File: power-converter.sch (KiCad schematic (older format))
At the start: 16 parts

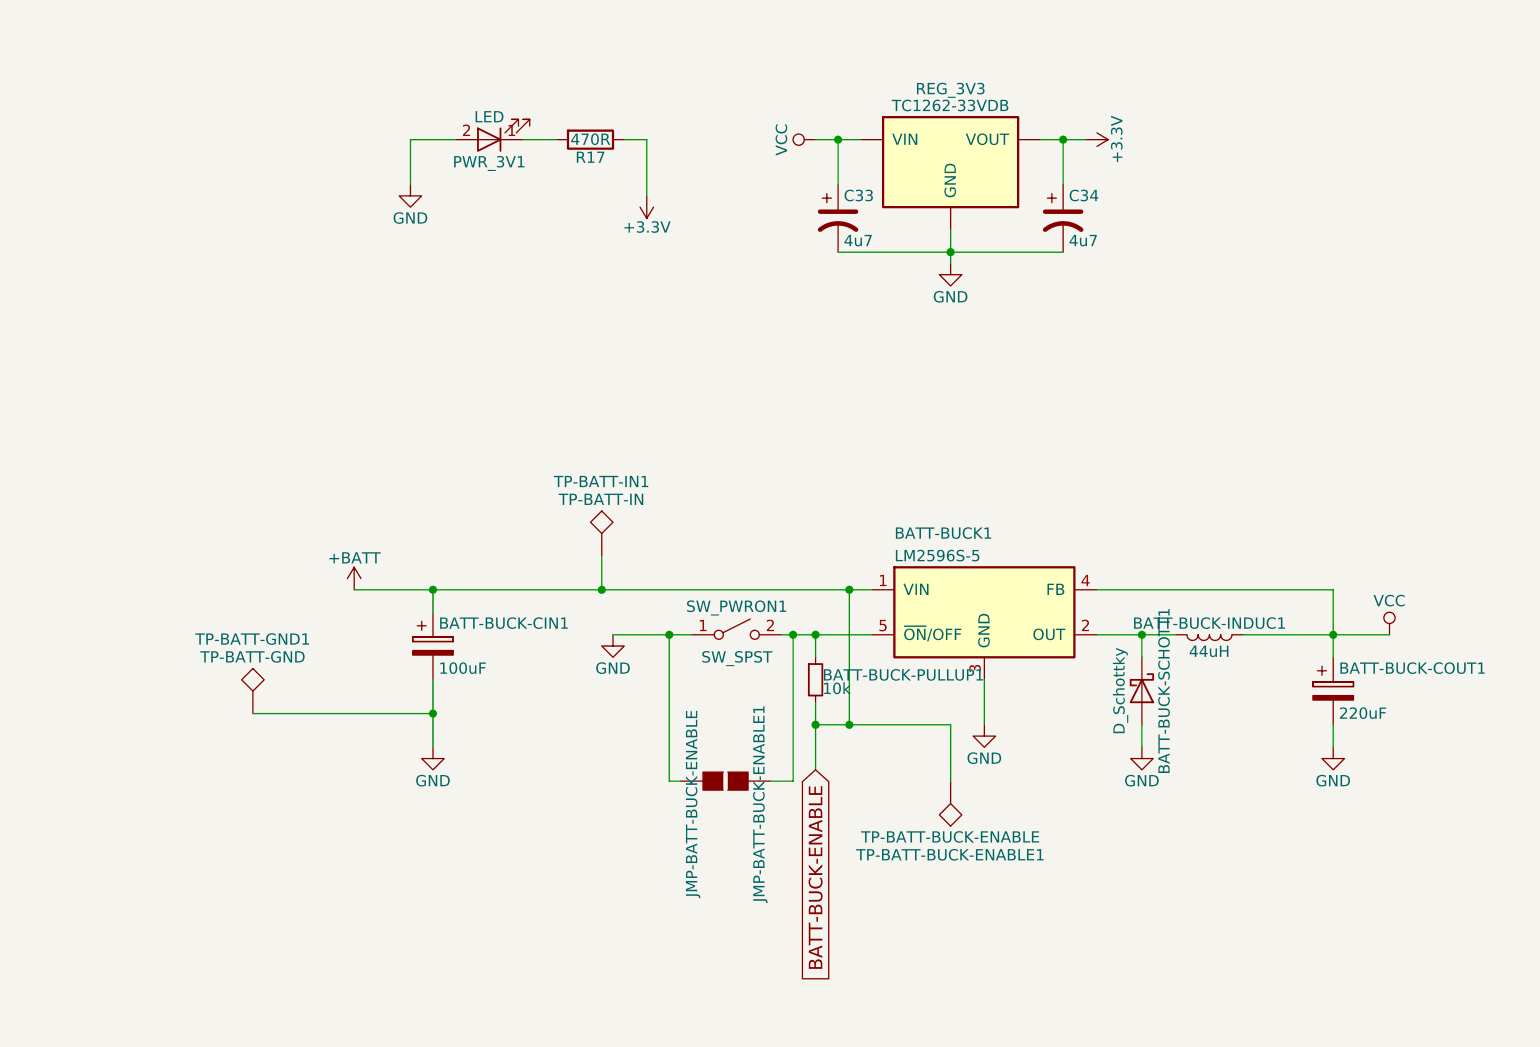
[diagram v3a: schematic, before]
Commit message: splitting led power out from 5v so that we can insert the mosfet
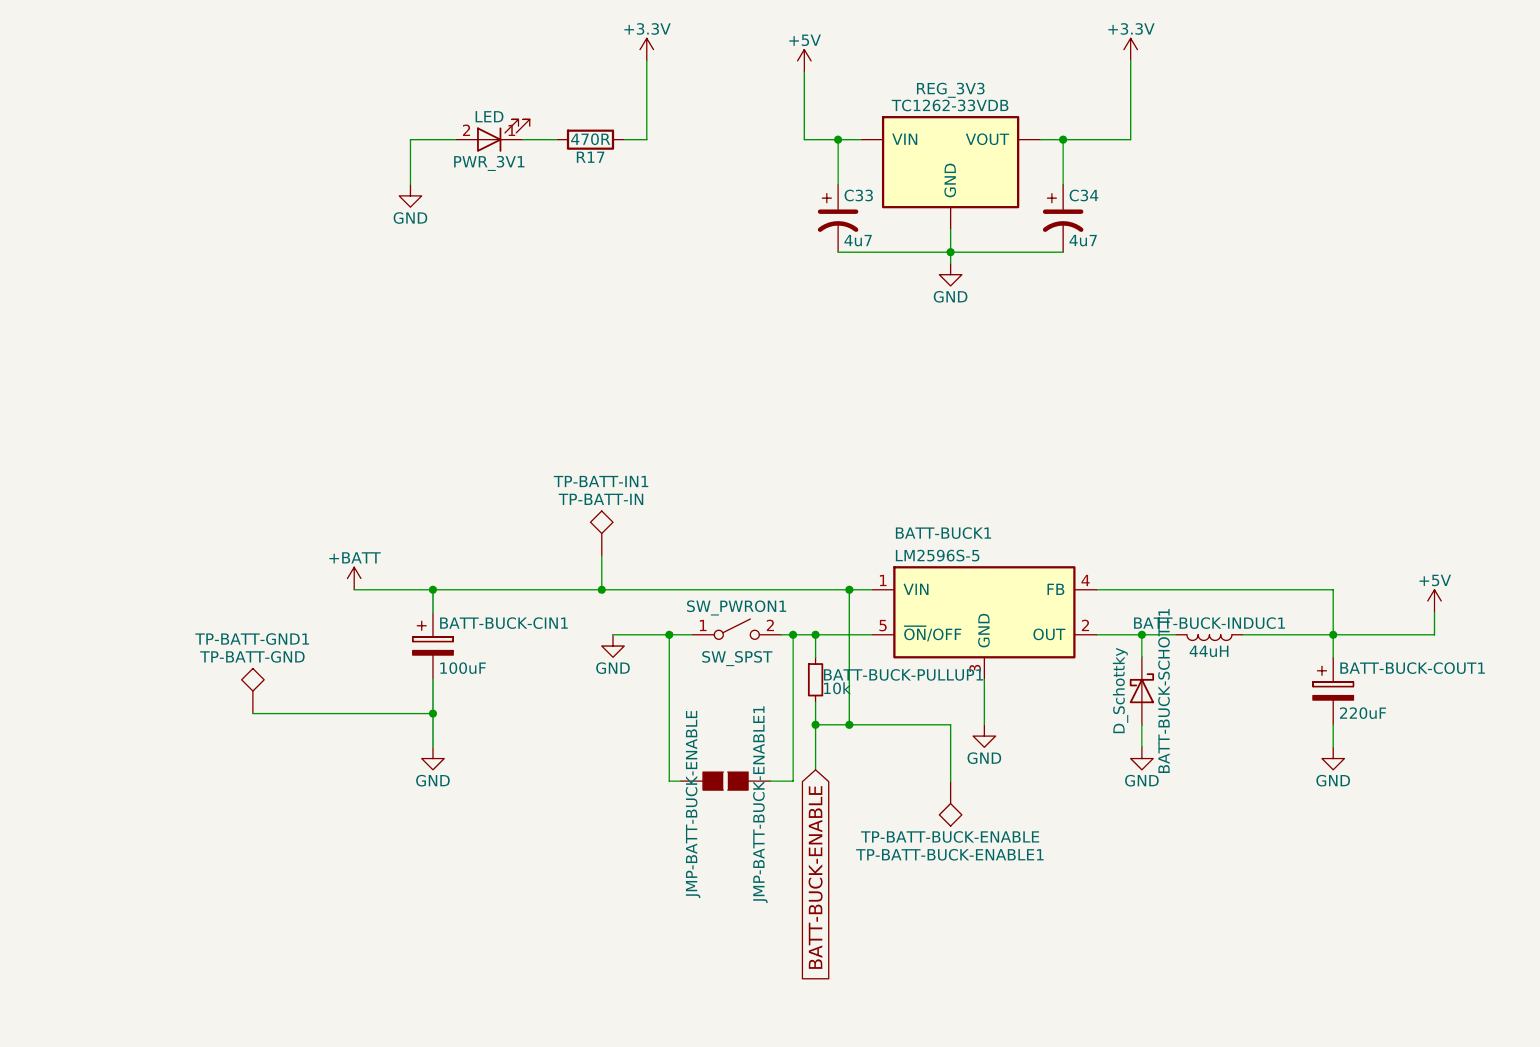
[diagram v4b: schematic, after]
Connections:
- net VCC renamed +5V
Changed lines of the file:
@@
 	5750 3900 6150 3900
 $Comp
-L GND #PWR025
+L GND #PWR27
 U 1 1 5B2D2C35
 P 5000 3900
-F 0 "#PWR025" H 5000 3650 50  0001 C CNN
+F 0 "#PWR27" H 5000 3650 50  0001 C CNN
 F 1 "GND" H 5000 3750 50  0000 C CNN
 F 2 "" H 5000 3900 50  0001 C CNN
@@
 Wire Wire Line
 	7150 3900 7500 3900
-$Comp
-L VCC #PWR026
-U 1 1 5B2D2C44
-P 8450 3900
-F 0 "#PWR026" H 8450 3750 50  0001 C CNN
-F 1 "VCC" H 8450 4050 50  0000 C CNN
-F 2 "" H 8450 3900 50  0001 C CNN
-F 3 "" H 8450 3900 50  0001 C CNN
-	1    8450 3900
-	1    0    0    -1
-$EndComp
-Wire Wire Line
-	7800 3900 8450 3900
+Wire Wire Line
+	7800 3900 8650 3900
 Wire Wire Line
 	7150 3700 8200 3700
@@
 Connection ~ 8200 3900
 $Comp
-L GND #PWR027
+L GND #PWR33
 U 1 1 5B2D2C55
 P 7350 4400
-F 0 "#PWR027" H 7350 4150 50  0001 C CNN
+F 0 "#PWR33" H 7350 4150 50  0001 C CNN
 F 1 "GND" H 7350 4250 50  0000 C CNN
 F 2 "" H 7350 4400 50  0001 C CNN
@@
 $EndComp
 $Comp
-L GND #PWR028
+L GND #PWR34
 U 1 1 5B2D2C63
 P 8200 4400
-F 0 "#PWR028" H 8200 4150 50  0001 C CNN
+F 0 "#PWR34" H 8200 4150 50  0001 C CNN
 F 1 "GND" H 8200 4250 50  0000 C CNN
 F 2 "" H 8200 4400 50  0001 C CNN
@@
 	8200 4300 8200 4400
 $Comp
-L GND #PWR029
+L GND #PWR31
 U 1 1 5B2D2C6A
 P 6650 4300
-F 0 "#PWR029" H 6650 4050 50  0001 C CNN
+F 0 "#PWR31" H 6650 4050 50  0001 C CNN
 F 1 "GND" H 6650 4150 50  0000 C CNN
 F 2 "" H 6650 4300 50  0001 C CNN
@@
 	3850 3700 6150 3700
 $Comp
-L GND #PWR030
+L GND #PWR26
 U 1 1 5B2D2C79
 P 4200 4400
-F 0 "#PWR030" H 4200 4150 50  0001 C CNN
+F 0 "#PWR26" H 4200 4150 50  0001 C CNN
 F 1 "GND" H 4200 4250 50  0000 C CNN
 F 2 "" H 4200 4400 50  0001 C CNN
@@
 Connection ~ 6050 4300
 $Comp
-L +BATT #PWR031
+L +BATT #PWR24
 U 1 1 5B2D2CA5
 P 3850 3700
-F 0 "#PWR031" H 3850 3550 50  0001 C CNN
+F 0 "#PWR24" H 3850 3550 50  0001 C CNN
 F 1 "+BATT" H 3850 3840 50  0000 C CNN
 F 2 "" H 3850 3700 50  0001 C CNN
@@
 Connection ~ 4200 4250
 $Comp
-L +3.3V #PWR032
+L +3.3V #PWR28
 U 1 1 5B2DAE29
-P 5150 1950
-F 0 "#PWR032" H 5150 1800 50  0001 C CNN
-F 1 "+3.3V" H 5150 2090 50  0000 C CNN
-F 2 "" H 5150 1950 50  0001 C CNN
-F 3 "" H 5150 1950 50  0001 C CNN
-	1    5150 1950
-	-1   0    0    1
+P 5150 1350
+F 0 "#PWR28" H 5150 1200 50  0001 C CNN
+F 1 "+3.3V" H 5150 1490 50  0000 C CNN
+F 2 "" H 5150 1350 50  0001 C CNN
+F 3 "" H 5150 1350 50  0001 C CNN
+	1    5150 1350
+	1    0    0    -1
 $EndComp
 $Comp
@@
 $EndComp
 $Comp
-L +3.3V #PWR033
+L +3.3V #PWR32
 U 1 1 5B2DAE36
-P 7100 1700
-F 0 "#PWR033" H 7100 1550 50  0001 C CNN
-F 1 "+3.3V" H 7100 1840 50  0000 C CNN
-F 2 "" H 7100 1700 50  0001 C CNN
-F 3 "" H 7100 1700 50  0001 C CNN
-	1    7100 1700
-	0    1    1    0
-$EndComp
-$Comp
-L VCC #PWR034
-U 1 1 5B2DAE3C
-P 5900 1700
-F 0 "#PWR034" H 5900 1550 50  0001 C CNN
-F 1 "VCC" H 5900 1850 50  0000 C CNN
-F 2 "" H 5900 1700 50  0001 C CNN
-F 3 "" H 5900 1700 50  0001 C CNN
-	1    5900 1700
-	0    -1   -1   0
-$EndComp
-$Comp
-L GND #PWR035
+P 7300 1350
+F 0 "#PWR32" H 7300 1200 50  0001 C CNN
+F 1 "+3.3V" H 7300 1490 50  0000 C CNN
+F 2 "" H 7300 1350 50  0001 C CNN
+F 3 "" H 7300 1350 50  0001 C CNN
+	1    7300 1350
+	1    0    0    -1
+$EndComp
+$Comp
+L GND #PWR30
 U 1 1 5B2DAE42
 P 6500 2250
-F 0 "#PWR035" H 6500 2000 50  0001 C CNN
+F 0 "#PWR30" H 6500 2000 50  0001 C CNN
 F 1 "GND" H 6500 2100 50  0000 C CNN
 F 2 "" H 6500 2250 50  0001 C CNN
@@
 $EndComp
 $Comp
-L GND #PWR036
+L GND #PWR25
 U 1 1 5B2DAE4F
 P 4100 1900
-F 0 "#PWR036" H 4100 1650 50  0001 C CNN
+F 0 "#PWR25" H 4100 1650 50  0001 C CNN
 F 1 "GND" H 4100 1750 50  0000 C CNN
 F 2 "" H 4100 1900 50  0001 C CNN
@@
 	6500 2100 6500 2250
 Wire Wire Line
-	5900 1700 6100 1700
-Wire Wire Line
-	6900 1700 7100 1700
+	5850 1700 6100 1700
+Wire Wire Line
+	6900 1700 7300 1700
 Wire Wire Line
 	4600 1700 4750 1700
-Wire Wire Line
-	5150 1700 5150 1950
 Wire Wire Line
 	5050 1700 5150 1700
@@
 	0    1    1    0
 $EndComp
+$Comp
+L +5V #PWR?
+U 1 1 5B114C95
+P 8650 3800
+F 0 "#PWR?" H 8650 3650 50  0001 C CNN
+F 1 "+5V" H 8650 3940 50  0000 C CNN
+F 2 "" H 8650 3800 50  0001 C CNN
+F 3 "" H 8650 3800 50  0001 C CNN
+	1    8650 3800
+	1    0    0    -1
+$EndComp
+Wire Wire Line
+	8650 3900 8650 3800
+$Comp
+L +5V #PWR?
+U 1 1 5B115086
+P 5850 1400
+F 0 "#PWR?" H 5850 1250 50  0001 C CNN
+F 1 "+5V" H 5850 1540 50  0000 C CNN
+F 2 "" H 5850 1400 50  0001 C CNN
+F 3 "" H 5850 1400 50  0001 C CNN
+	1    5850 1400
+	1    0    0    -1
+$EndComp
+Wire Wire Line
+	5850 1400 5850 1700
+Wire Wire Line
+	7300 1700 7300 1350
+Wire Wire Line
+	5150 1700 5150 1350
 $EndSCHEMATC

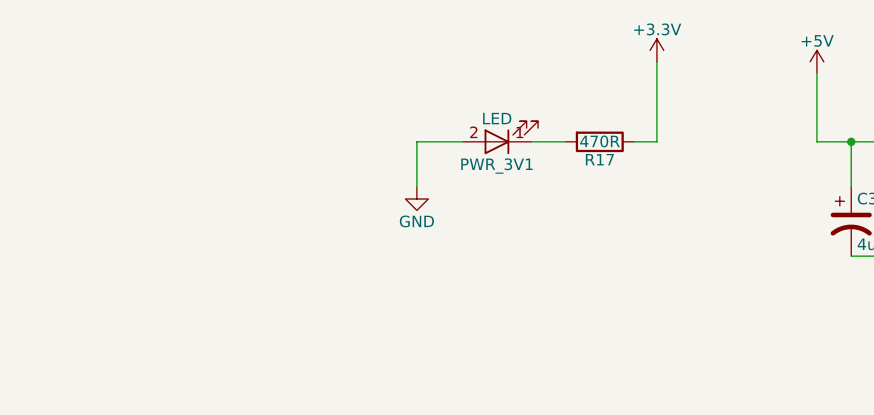
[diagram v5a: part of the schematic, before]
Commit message: Add leds for the three power planes
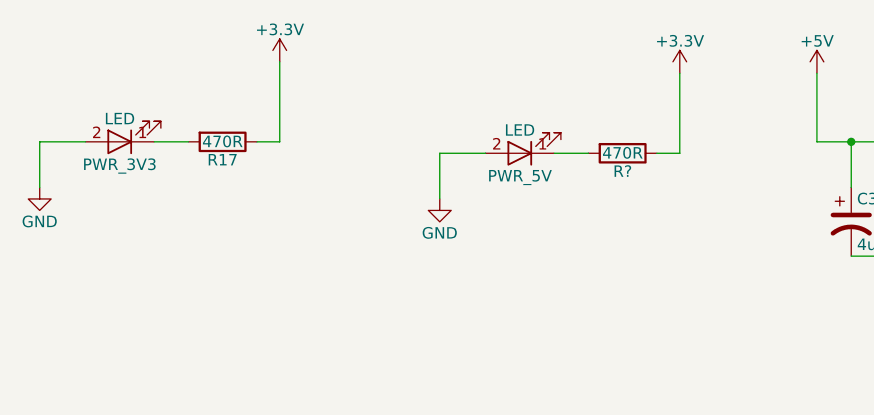
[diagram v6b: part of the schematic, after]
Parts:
- added PWR_5V: LED, LEDs:LED_0603, symbol LED
- added R?: 470R, Resistors_SMD:R_0603, symbol R
- renumbered PWR_3V1 to PWR_3V3
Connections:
- net +3V3: now also R?.1
- net GND: now also PWR_5V.2 (A)
- new net: PWR_5V.1 (K), R?.2
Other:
- moved on the sheet: PWR_3V3, R17
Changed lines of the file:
@@
 L +3.3V #PWR28
 U 1 1 5B2DAE29
-P 5150 1350
-F 0 "#PWR28" H 5150 1200 50  0001 C CNN
-F 1 "+3.3V" H 5150 1490 50  0000 C CNN
-F 2 "" H 5150 1350 50  0001 C CNN
-F 3 "" H 5150 1350 50  0001 C CNN
-	1    5150 1350
+P 3500 1350
+F 0 "#PWR28" H 3500 1200 50  0001 C CNN
+F 1 "+3.3V" H 3500 1490 50  0000 C CNN
+F 2 "" H 3500 1350 50  0001 C CNN
+F 3 "" H 3500 1350 50  0001 C CNN
+	1    3500 1350
 	1    0    0    -1
 $EndComp
@@
 L R R17
 U 1 1 5B2DAE48
-P 4900 1700
-F 0 "R17" V 4980 1700 50  0000 C CNN
-F 1 "470R" V 4900 1700 50  0000 C CNN
-F 2 "Resistors_SMD:R_0603" V 4830 1700 50  0001 C CNN
-F 3 "" H 4900 1700 50  0001 C CNN
-	1    4900 1700
+P 3250 1700
+F 0 "R17" V 3330 1700 50  0000 C CNN
+F 1 "470R" V 3250 1700 50  0000 C CNN
+F 2 "Resistors_SMD:R_0603" V 3180 1700 50  0001 C CNN
+F 3 "" H 3250 1700 50  0001 C CNN
+	1    3250 1700
 	0    1    1    0
 $EndComp
@@
 L GND #PWR25
 U 1 1 5B2DAE4F
-P 4100 1900
-F 0 "#PWR25" H 4100 1650 50  0001 C CNN
-F 1 "GND" H 4100 1750 50  0000 C CNN
-F 2 "" H 4100 1900 50  0001 C CNN
-F 3 "" H 4100 1900 50  0001 C CNN
-	1    4100 1900
-	1    0    0    -1
-$EndComp
-$Comp
-L LED PWR_3V1
+P 2450 1900
+F 0 "#PWR25" H 2450 1650 50  0001 C CNN
+F 1 "GND" H 2450 1750 50  0000 C CNN
+F 2 "" H 2450 1900 50  0001 C CNN
+F 3 "" H 2450 1900 50  0001 C CNN
+	1    2450 1900
+	1    0    0    -1
+$EndComp
+$Comp
+L LED PWR_3V3
 U 1 1 5B2DAE55
-P 4450 1700
-F 0 "PWR_3V1" H 4450 1800 50  0000 C CNN
-F 1 "LED" H 4450 1600 50  0000 C CNN
-F 2 "LEDs:LED_0603" H 4450 1700 50  0001 C CNN
-F 3 "" H 4450 1700 50  0001 C CNN
-	1    4450 1700
+P 2800 1700
+F 0 "PWR_3V3" H 2800 1800 50  0000 C CNN
+F 1 "LED" H 2800 1600 50  0000 C CNN
+F 2 "LEDs:LED_0603" H 2800 1700 50  0001 C CNN
+F 3 "" H 2800 1700 50  0001 C CNN
+	1    2800 1700
 	-1   0    0    1
 $EndComp
@@
 	6900 1700 7300 1700
 Wire Wire Line
-	4600 1700 4750 1700
-Wire Wire Line
-	5050 1700 5150 1700
-Wire Wire Line
-	4100 1700 4100 1900
-Wire Wire Line
-	4300 1700 4100 1700
+	2950 1700 3100 1700
+Wire Wire Line
+	3400 1700 3500 1700
+Wire Wire Line
+	2450 1700 2450 1900
+Wire Wire Line
+	2650 1700 2450 1700
 Wire Wire Line
 	7000 1900 7000 1700
@@
 	7300 1700 7300 1350
 Wire Wire Line
-	5150 1700 5150 1350
+	3500 1700 3500 1350
+$Comp
+L +3.3V #PWR?
+U 1 1 5B16EDF6
+P 5250 1400
+F 0 "#PWR?" H 5250 1250 50  0001 C CNN
+F 1 "+3.3V" H 5250 1540 50  0000 C CNN
+F 2 "" H 5250 1400 50  0001 C CNN
+F 3 "" H 5250 1400 50  0001 C CNN
+	1    5250 1400
+	1    0    0    -1
+$EndComp
+$Comp
+L R R?
+U 1 1 5B16EDFC
+P 5000 1750
+F 0 "R?" V 5080 1750 50  0000 C CNN
+F 1 "470R" V 5000 1750 50  0000 C CNN
+F 2 "Resistors_SMD:R_0603" V 4930 1750 50  0001 C CNN
+F 3 "" H 5000 1750 50  0001 C CNN
+	1    5000 1750
+	0    1    1    0
+$EndComp
+$Comp
+L GND #PWR?
+U 1 1 5B16EE02
+P 4200 1950
+F 0 "#PWR?" H 4200 1700 50  0001 C CNN
+F 1 "GND" H 4200 1800 50  0000 C CNN
+F 2 "" H 4200 1950 50  0001 C CNN
+F 3 "" H 4200 1950 50  0001 C CNN
+	1    4200 1950
+	1    0    0    -1
+$EndComp
+$Comp
+L LED PWR_5V
+U 1 1 5B16EE08
+P 4550 1750
+F 0 "PWR_5V" H 4550 1850 50  0000 C CNN
+F 1 "LED" H 4550 1650 50  0000 C CNN
+F 2 "LEDs:LED_0603" H 4550 1750 50  0001 C CNN
+F 3 "" H 4550 1750 50  0001 C CNN
+	1    4550 1750
+	-1   0    0    1
+$EndComp
+Wire Wire Line
+	4700 1750 4850 1750
+Wire Wire Line
+	5150 1750 5250 1750
+Wire Wire Line
+	4200 1750 4200 1950
+Wire Wire Line
+	4400 1750 4200 1750
+Wire Wire Line
+	5250 1750 5250 1400
 $EndSCHEMATC

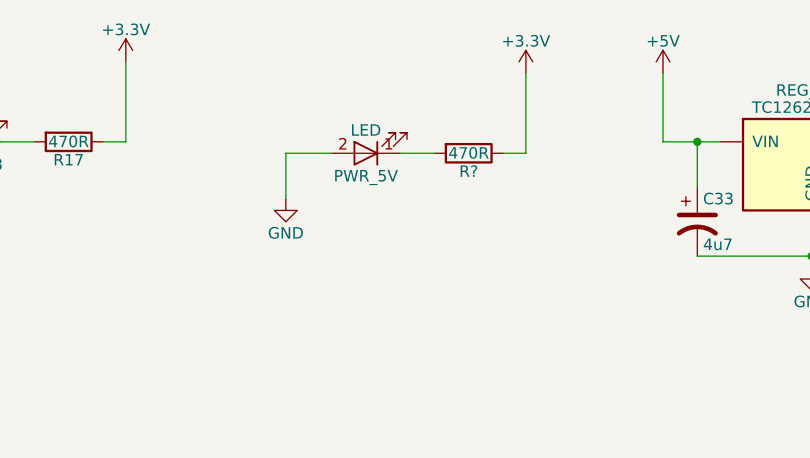
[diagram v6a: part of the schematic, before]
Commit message: Futher cleanup and footprint work, as well as power circuit fixes
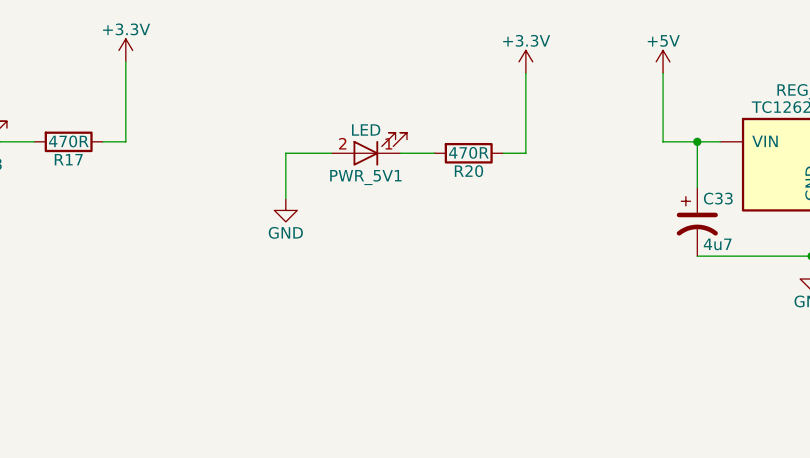
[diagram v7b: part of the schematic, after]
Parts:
- gave numbers to parts that had none: 1
- renumbered PWR_5V to PWR_5V1
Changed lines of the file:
@@
 	5750 3900 6150 3900
 $Comp
-L GND #PWR27
+L GND #PWR29
 U 1 1 5B2D2C35
 P 5000 3900
-F 0 "#PWR27" H 5000 3650 50  0001 C CNN
+F 0 "#PWR29" H 5000 3650 50  0001 C CNN
 F 1 "GND" H 5000 3750 50  0000 C CNN
 F 2 "" H 5000 3900 50  0001 C CNN
@@
 Connection ~ 8200 3900
 $Comp
-L GND #PWR33
+L GND #PWR35
 U 1 1 5B2D2C55
 P 7350 4400
-F 0 "#PWR33" H 7350 4150 50  0001 C CNN
+F 0 "#PWR35" H 7350 4150 50  0001 C CNN
 F 1 "GND" H 7350 4250 50  0000 C CNN
 F 2 "" H 7350 4400 50  0001 C CNN
@@
 $EndComp
 $Comp
-L GND #PWR34
+L GND #PWR36
 U 1 1 5B2D2C63
 P 8200 4400
-F 0 "#PWR34" H 8200 4150 50  0001 C CNN
+F 0 "#PWR36" H 8200 4150 50  0001 C CNN
 F 1 "GND" H 8200 4250 50  0000 C CNN
 F 2 "" H 8200 4400 50  0001 C CNN
@@
 	8200 4300 8200 4400
 $Comp
-L GND #PWR31
+L GND #PWR33
 U 1 1 5B2D2C6A
 P 6650 4300
-F 0 "#PWR31" H 6650 4050 50  0001 C CNN
+F 0 "#PWR33" H 6650 4050 50  0001 C CNN
 F 1 "GND" H 6650 4150 50  0000 C CNN
 F 2 "" H 6650 4300 50  0001 C CNN
@@
 	3850 3700 6150 3700
 $Comp
-L GND #PWR26
+L GND #PWR28
 U 1 1 5B2D2C79
 P 4200 4400
-F 0 "#PWR26" H 4200 4150 50  0001 C CNN
+F 0 "#PWR28" H 4200 4150 50  0001 C CNN
 F 1 "GND" H 4200 4250 50  0000 C CNN
 F 2 "" H 4200 4400 50  0001 C CNN
@@
 Connection ~ 6050 4300
 $Comp
-L +BATT #PWR24
+L +BATT #PWR26
 U 1 1 5B2D2CA5
 P 3850 3700
-F 0 "#PWR24" H 3850 3550 50  0001 C CNN
+F 0 "#PWR26" H 3850 3550 50  0001 C CNN
 F 1 "+BATT" H 3850 3840 50  0000 C CNN
 F 2 "" H 3850 3700 50  0001 C CNN
@@
 Connection ~ 4200 4250
 $Comp
-L +3.3V #PWR28
+L +3.3V #PWR25
 U 1 1 5B2DAE29
 P 3500 1350
-F 0 "#PWR28" H 3500 1200 50  0001 C CNN
+F 0 "#PWR25" H 3500 1200 50  0001 C CNN
 F 1 "+3.3V" H 3500 1490 50  0000 C CNN
 F 2 "" H 3500 1350 50  0001 C CNN
@@
 $EndComp
 $Comp
-L +3.3V #PWR32
+L +3.3V #PWR34
 U 1 1 5B2DAE36
 P 7300 1350
-F 0 "#PWR32" H 7300 1200 50  0001 C CNN
+F 0 "#PWR34" H 7300 1200 50  0001 C CNN
 F 1 "+3.3V" H 7300 1490 50  0000 C CNN
 F 2 "" H 7300 1350 50  0001 C CNN
@@
 $EndComp
 $Comp
-L GND #PWR30
+L GND #PWR32
 U 1 1 5B2DAE42
 P 6500 2250
-F 0 "#PWR30" H 6500 2000 50  0001 C CNN
+F 0 "#PWR32" H 6500 2000 50  0001 C CNN
 F 1 "GND" H 6500 2100 50  0000 C CNN
 F 2 "" H 6500 2250 50  0001 C CNN
@@
 $EndComp
 $Comp
-L GND #PWR25
+L GND #PWR24
 U 1 1 5B2DAE4F
 P 2450 1900
-F 0 "#PWR25" H 2450 1650 50  0001 C CNN
+F 0 "#PWR24" H 2450 1650 50  0001 C CNN
 F 1 "GND" H 2450 1750 50  0000 C CNN
 F 2 "" H 2450 1900 50  0001 C CNN
@@
 $EndComp
 $Comp
-L +5V #PWR35
+L +5V #PWR37
 U 1 1 5B114C95
 P 8650 3800
-F 0 "#PWR35" H 8650 3650 50  0001 C CNN
+F 0 "#PWR37" H 8650 3650 50  0001 C CNN
 F 1 "+5V" H 8650 3940 50  0000 C CNN
 F 2 "" H 8650 3800 50  0001 C CNN
@@
 	8650 3900 8650 3800
 $Comp
-L +5V #PWR29
+L +5V #PWR31
 U 1 1 5B115086
 P 5850 1400
-F 0 "#PWR29" H 5850 1250 50  0001 C CNN
+F 0 "#PWR31" H 5850 1250 50  0001 C CNN
 F 1 "+5V" H 5850 1540 50  0000 C CNN
 F 2 "" H 5850 1400 50  0001 C CNN
@@
 	3500 1700 3500 1350
 $Comp
-L +3.3V #PWR?
+L +3.3V #PWR30
 U 1 1 5B16EDF6
 P 5250 1400
-F 0 "#PWR?" H 5250 1250 50  0001 C CNN
+F 0 "#PWR30" H 5250 1250 50  0001 C CNN
 F 1 "+3.3V" H 5250 1540 50  0000 C CNN
 F 2 "" H 5250 1400 50  0001 C CNN
@@
 $EndComp
 $Comp
-L R R?
+L R R20
 U 1 1 5B16EDFC
 P 5000 1750
-F 0 "R?" V 5080 1750 50  0000 C CNN
+F 0 "R20" V 5080 1750 50  0000 C CNN
 F 1 "470R" V 5000 1750 50  0000 C CNN
 F 2 "Resistors_SMD:R_0603" V 4930 1750 50  0001 C CNN
@@
 $EndComp
 $Comp
-L GND #PWR?
+L GND #PWR27
 U 1 1 5B16EE02
 P 4200 1950
-F 0 "#PWR?" H 4200 1700 50  0001 C CNN
+F 0 "#PWR27" H 4200 1700 50  0001 C CNN
 F 1 "GND" H 4200 1800 50  0000 C CNN
 F 2 "" H 4200 1950 50  0001 C CNN
@@
 $EndComp
 $Comp
-L LED PWR_5V
+L LED PWR_5V1
 U 1 1 5B16EE08
 P 4550 1750
-F 0 "PWR_5V" H 4550 1850 50  0000 C CNN
+F 0 "PWR_5V1" H 4550 1850 50  0000 C CNN
 F 1 "LED" H 4550 1650 50  0000 C CNN
 F 2 "LEDs:LED_0603" H 4550 1750 50  0001 C CNN
